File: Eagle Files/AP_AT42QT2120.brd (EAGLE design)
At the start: 36 x 36.5 mm, 20 parts, among them U2 AT42QT2120

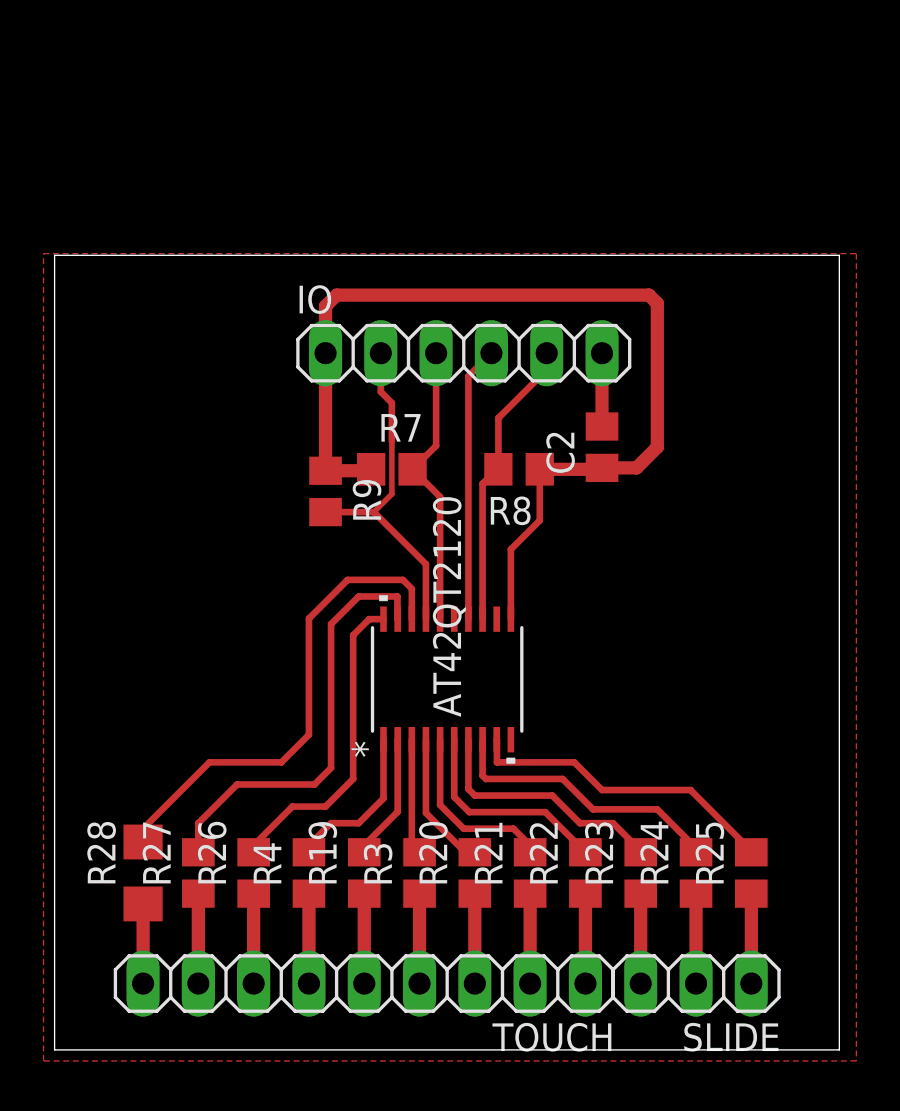
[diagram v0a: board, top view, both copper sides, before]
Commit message: v2 with larger packages
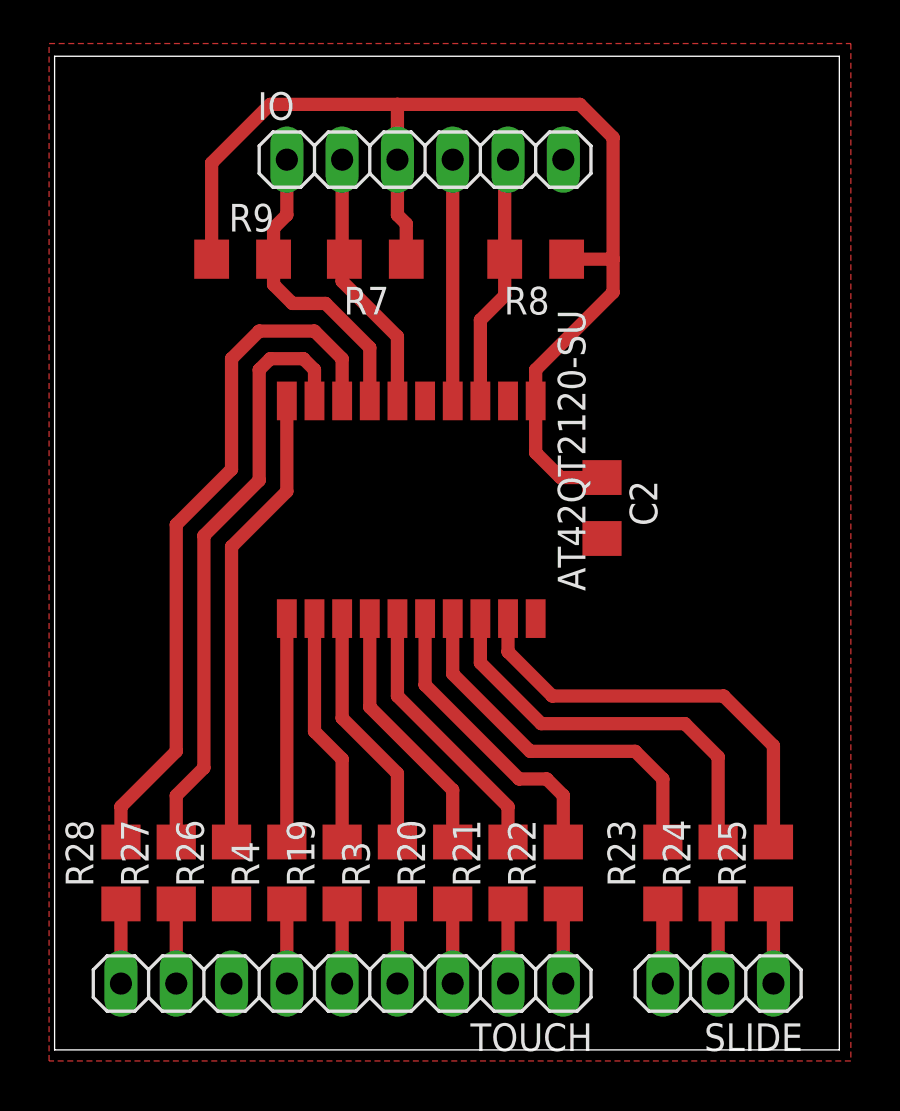
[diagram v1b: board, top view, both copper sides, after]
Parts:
- removed U2: AT42QT2120, 2022-03-29_19-48-10_Library:TSSOP20_MC_MCH-L
- added U$1: AT42QT2120-SU, 2022-03-29_19-48-10_Library:SOIC20
- C2: device rcl:C0805 -> rcl:C1206
- R19, R20, R21, R22, R23, R24, R25, R26, R27, R3, R4, R7, R8, R9: device rcl:R0805 -> rcl:R1206
- moved R9 11.3 mm to (8.64, 36.3), turned to 0 degrees
- moved R7 9.68 mm to (14.7, 36.3), turned to 180 degrees
- moved R8 9.68 mm to (22.1, 36.3)
- moved IO 9.07 mm to (17.0, 40.9)
- moved C2 2.79 mm to (25.1, 24.9), turned to 270 degrees
- moved R25 1.02 mm to (33.0, 8.13)
- moved R21 1.02 mm to (20.8, 8.13)
- moved R22 1.02 mm to (23.4, 8.13)
- moved R23 1.02 mm to (27.9, 8.13)
- moved R24 1.02 mm to (30.5, 8.13)
- moved SLIDE 1.02 mm to (30.5, 3.05)
- moved R19 1.02 mm to (13.2, 8.13)
- moved R26 1.02 mm to (8.13, 8.13)
- moved R27 1.02 mm to (5.59, 8.13)
- moved R28 1.02 mm to (3.05, 8.13)
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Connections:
- removed net N$19 (its old number): R26.2, U2.20
- removed net N$23: R27.2, U2.19
- new net N$20: R26.2, U$1.20
- new net N$29: R28.2, U$1.18
- net +3V3: now also IO.3, U$1.11; no longer IO.1, U2.11
- net GND: now also U$1.10, U$1.12; no longer U2.10, U2.12
- net N$1: now also U$1.1; no longer U2.1
- net N$2: now also U$1.2; no longer U2.2
- net N$24: now also R27.2, U$1.19; no longer R28.2, U2.18
- net N$25: now also IO.2, U$1.16; no longer IO.3, U2.16
- net N$26: now also IO.1, U$1.17; no longer IO.2, U2.17
- net N$27: now also U$1.13; no longer U2.13
- net N$28: now also U$1.14; no longer U2.14
- net N$3: now also U$1.3; no longer U2.3
- net N$4: now also U$1.4; no longer U2.4
- net N$5: now also U$1.5; no longer U2.5
- net N$6: now also U$1.6; no longer U2.6
- net N$7: now also U$1.7; no longer U2.7
- net N$8: now also U$1.8; no longer U2.8
- net N$9: now also U$1.9; no longer U2.9
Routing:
- net N$29: track 0.00 -> 32.7 mm
- net N$20: track 0.00 -> 21.3 mm
- net N$23: track 19.7 -> 0.00 mm
- net N$19 (its old number): track 14.5 -> 0.00 mm
- net +3V3: track 45.8 -> 53.5 mm
- net N$24: track 22.4 -> 28.4 mm
- net N$3: track 5.32 -> 11.3 mm
- net N$7: track 11.7 -> 17.3 mm
- net N$8: track 13.0 -> 18.7 mm
- net N$9: track 14.7 -> 19.9 mm
- net N$4: track 7.00 -> 11.8 mm
- net N$2: track 6.00 -> 10.8 mm
- net N$5: track 8.22 -> 12.4 mm
- net N$19: track 4.13 -> 0.00 mm
- net N$6: track 9.71 -> 13.6 mm
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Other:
- board size 36 x 36.5 mm -> 36 x 45.6 mm

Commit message: pcb changes
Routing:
- net GND: track 0.00 -> 26.9 mm
- net N$19: track 0.00 -> 3.66 mm
- removed copper zone on layer 1, net GND
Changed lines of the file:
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@@
 <contactref element="C2" pad="2"/>
 <contactref element="IO" pad="6"/>
-<polygon width="0.3048" layer="1">
-<vertex x="-0.254" y="-0.508"/>
-<vertex x="-0.254" y="46.228"/>
-<vertex x="36.576" y="46.228"/>
-<vertex x="36.576" y="-0.508"/>
-</polygon>
 <contactref element="U$1" pad="12"/>
 <contactref element="U$1" pad="10"/>
+<wire x1="23.368" y1="40.894" x2="23.368" y2="39.624" width="0.6096" layer="1"/>
+<wire x1="23.368" y1="39.624" x2="22.098" y2="38.354" width="0.6096" layer="1"/>
+<wire x1="22.098" y1="38.354" x2="22.098" y2="33.274" width="0.6096" layer="1"/>
+<wire x1="22.098" y1="33.274" x2="20.828" y2="32.004" width="0.6096" layer="1"/>
+<wire x1="20.828" y1="32.004" x2="20.828" y2="29.812" width="0.6096" layer="1"/>
+<wire x1="20.828" y1="29.812" x2="20.828" y2="26.67" width="0.6096" layer="1"/>
+<wire x1="24.006" y1="23.492" x2="25.146" y2="23.492" width="0.6096" layer="1"/>
+<wire x1="20.828" y1="26.67" x2="24.006" y2="23.492" width="0.6096" layer="1"/>
+<wire x1="22.098" y1="19.812" x2="23.876" y2="19.812" width="0.6096" layer="1"/>
+<wire x1="23.876" y1="19.812" x2="25.146" y2="21.082" width="0.6096" layer="1"/>
+<wire x1="25.146" y1="21.082" x2="25.146" y2="23.492" width="0.6096" layer="1"/>
 </signal>
 <signal name="+3V3">
@@
 <contactref element="TOUCH" pad="7"/>
 <contactref element="R26" pad="1"/>
-<wire x1="8.128" y1="3.048" x2="8.128" y2="6.706" width="0" layer="19" extent="1-1"/>
+<wire x1="8.128" y1="3.048" x2="8.128" y2="6.706" width="0.6096" layer="1"/>
 </signal>
 <signal name="N$20">
